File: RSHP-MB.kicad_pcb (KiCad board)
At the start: 2 copper layers, 120 x 120 mm, 23 parts, among them J1 Conn_02x20_Odd_Even, J2 Conn_02x02_Odd_Even, J3 Conn_02x02_Odd_Even, J4 Conn_02x04_Odd_Even

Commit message: Properly filled document metadata
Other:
- board text removed: "RSHP-CB-0010"
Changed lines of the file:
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@@
   )
   (paper "A4")
+  (title_block
+    (title "RSHP-CB-0010")
+    (date "2022-05-21")
+    (rev "1.0")
+    (company "(c) Andriy Golovnya http://redscorp.net")
+    (comment 1 "Reflow Soldering Hot Plate - Mounting Board")
+  )
   (layers
     (0 "F.Cu" signal)
@@
     (effects (font (size 1.5 1.5) (thickness 0.3)) (justify mirror))
   )
-  (gr_text "RSHP-CB-0010" (at 187.5 190) (layer "User.1")
-    (effects (font (size 1 1) (thickness 0.15)) (justify left))
-  )
   (via (at 52.5 110) (size 0.8) (drill 0.4) (layers "F.Cu" "B.Cu") (free) (net 3))

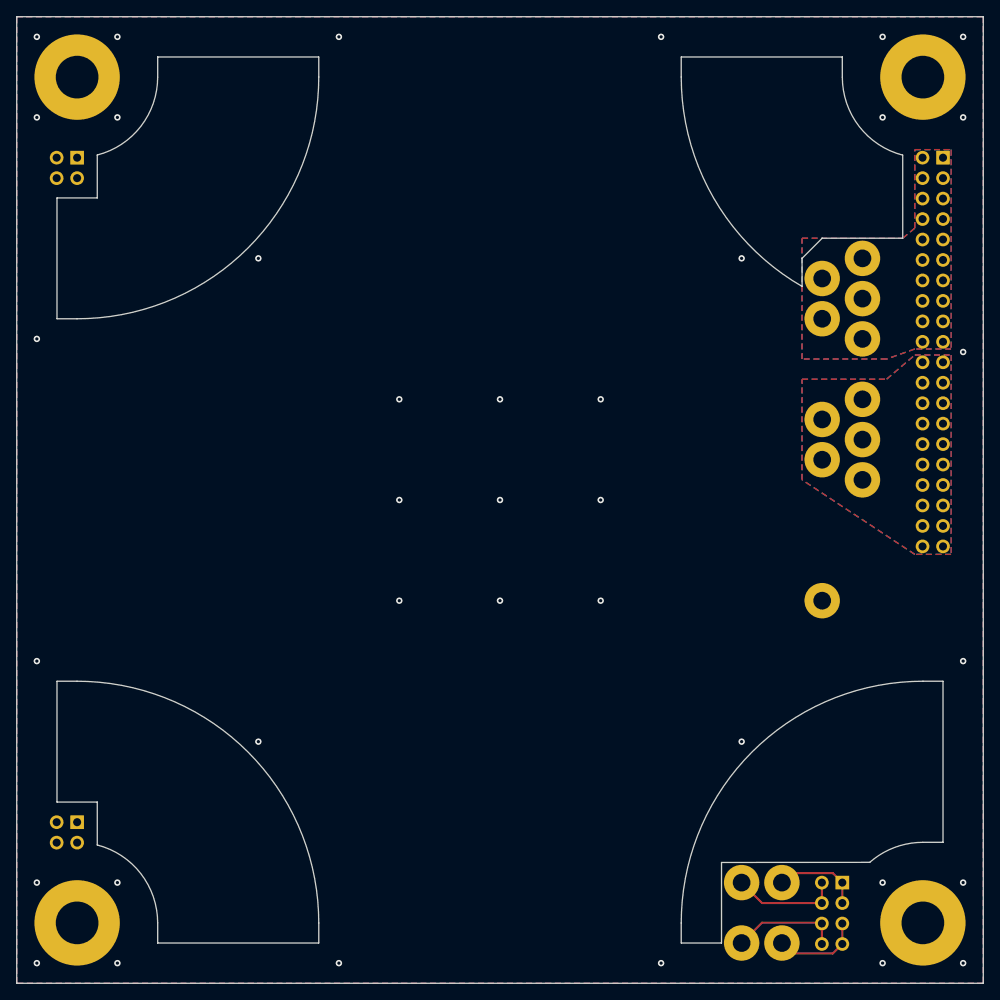
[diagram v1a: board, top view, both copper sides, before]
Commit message: Switched TR connector sides in schematics. rounded some corners on PCB.
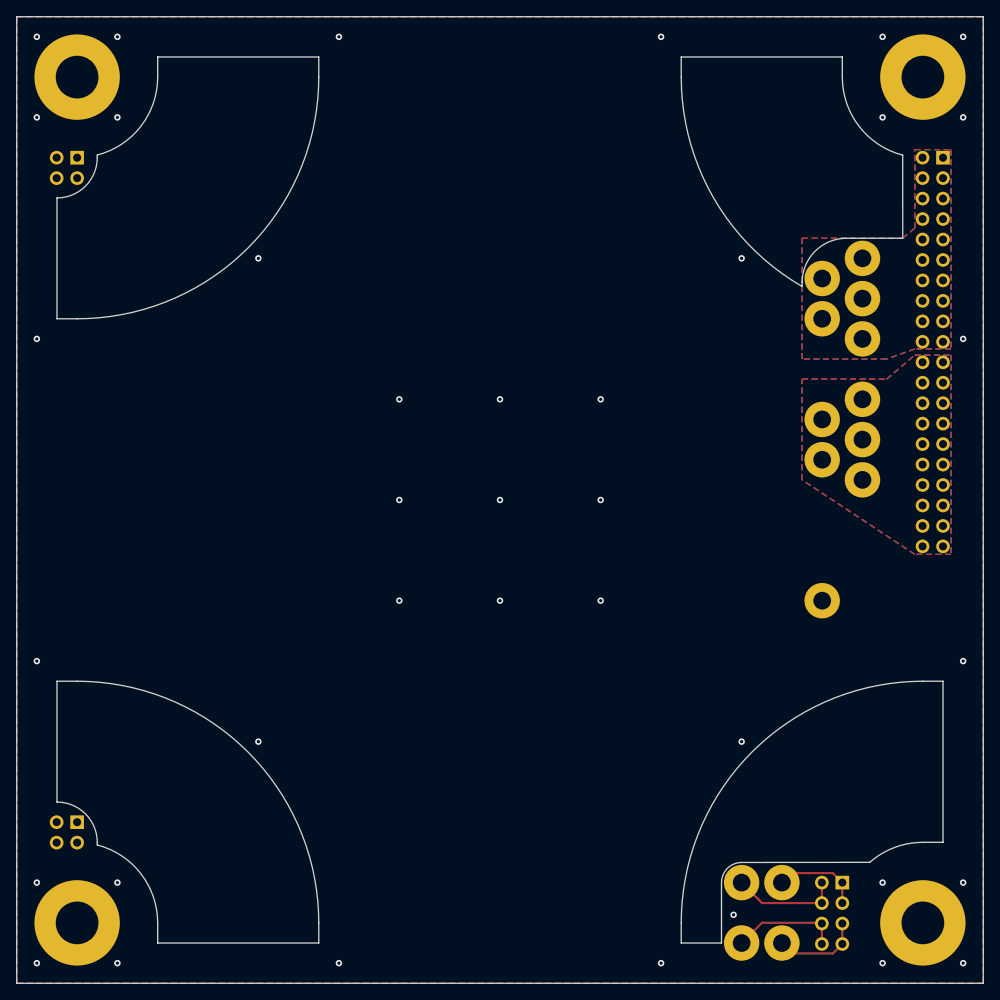
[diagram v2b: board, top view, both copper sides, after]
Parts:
- moved H16 5.00 mm to (140.0, 137.5)
- moved H17 5.00 mm to (145.0, 137.5)
- moved H18 5.00 mm to (140.0, 145.0)
- moved H19 5.00 mm to (145.0, 145.0)
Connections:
- J4 pad 1: TR1_VCC -> TR1_GND
- J4 pad 2: TR1_GND -> TR1_VCC
- J4 pad 3: TR1_VCC -> TR1_GND
- J4 pad 4: TR1_GND -> TR1_VCC
- J4 pad 5: TR2_VCC -> TR2_GND
- J4 pad 6: TR2_GND -> TR2_VCC
- J4 pad 7: TR2_VCC -> TR2_GND
- J4 pad 8: TR2_GND -> TR2_VCC
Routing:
- net TR2_VCC: track 11.6 -> 13.6 mm
- net TR2_GND: track 13.6 -> 11.6 mm
- net TR1_VCC: track 11.6 -> 13.6 mm
- net TR1_GND: track 13.6 -> 11.6 mm
- net EARTH: vias 37 -> 38
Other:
- outline, holes or cut-outs redrawn
